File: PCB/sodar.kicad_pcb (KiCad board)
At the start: 2 copper layers, 70 parts, among them J1 Screw_Terminal_01x02, J2 Conn_02x12_Counter_Clockwise, J3 Conn_01x02, U1 TC78H621FNG, U10 TC78H621FNG, U2 TC78H621FNG, U3 TC78H621FNG, U4 TC78H621FNG, U5 TC78H621FNG, U6 TC78H621FNG, U7 TC78H621FNG, U8 TC78H621FNG, U9 TC78H621FNG

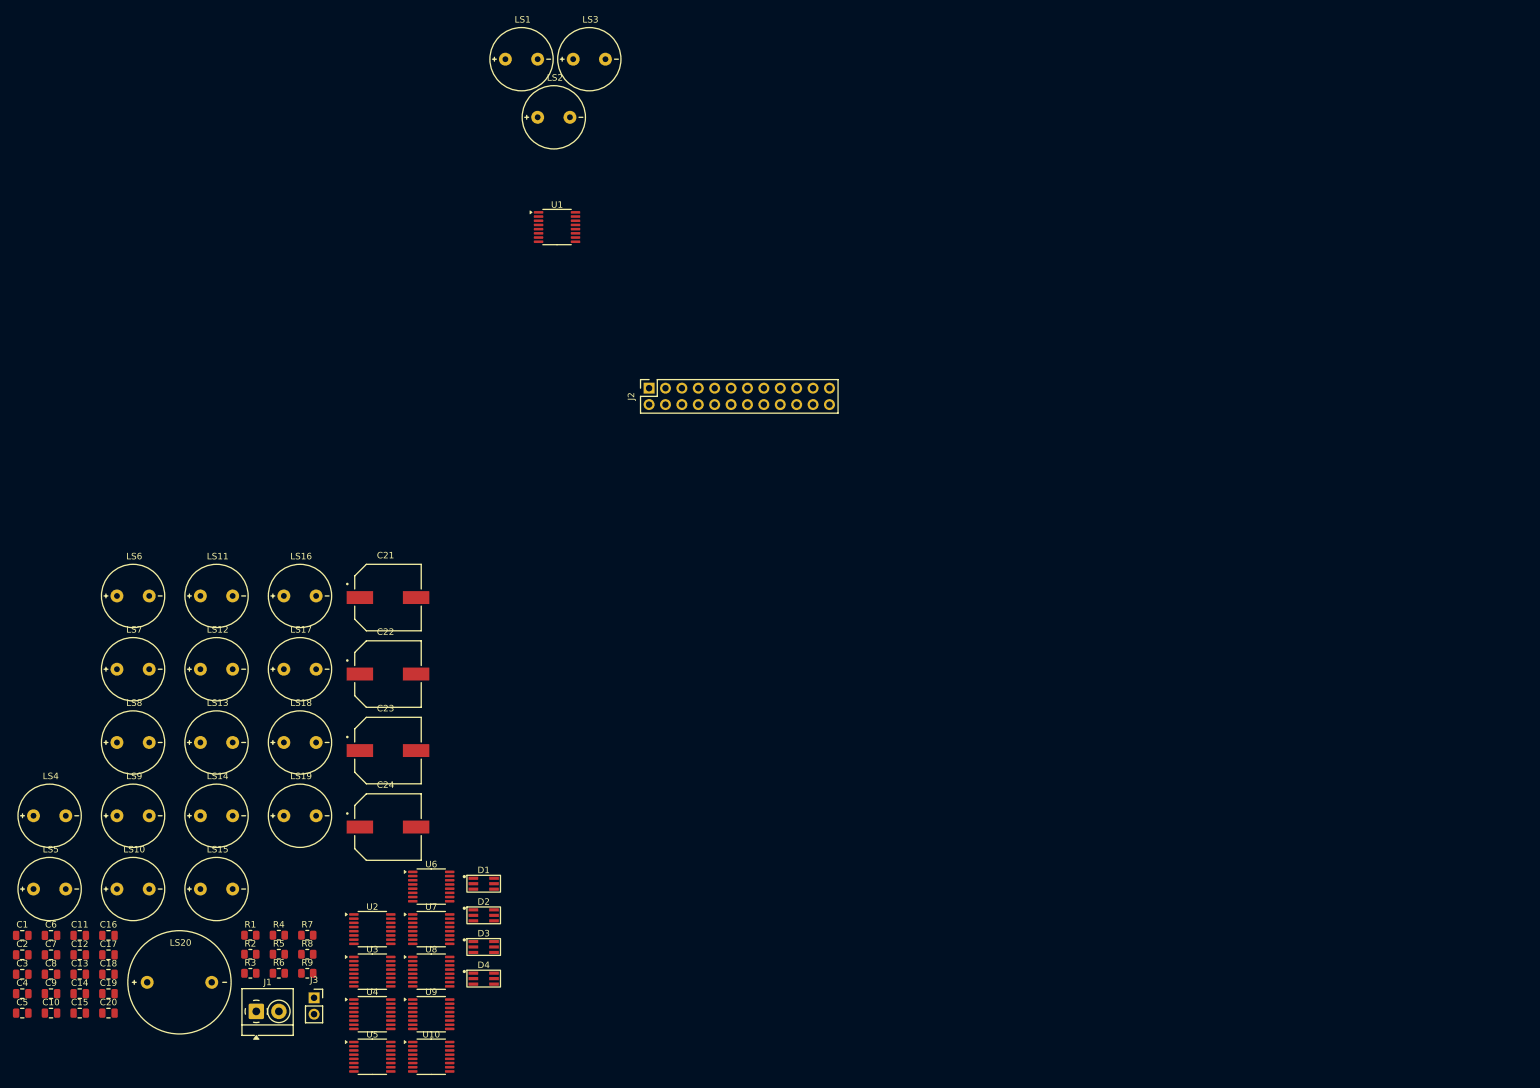
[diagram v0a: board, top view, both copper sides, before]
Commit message: Szymi pcb design (#5)
* updated transmiter footprint

* Moved the transducers and the drivers in the right positions

* first PCB layout finished, to be reviewed

---------

Co-authored-by: ads <ads>
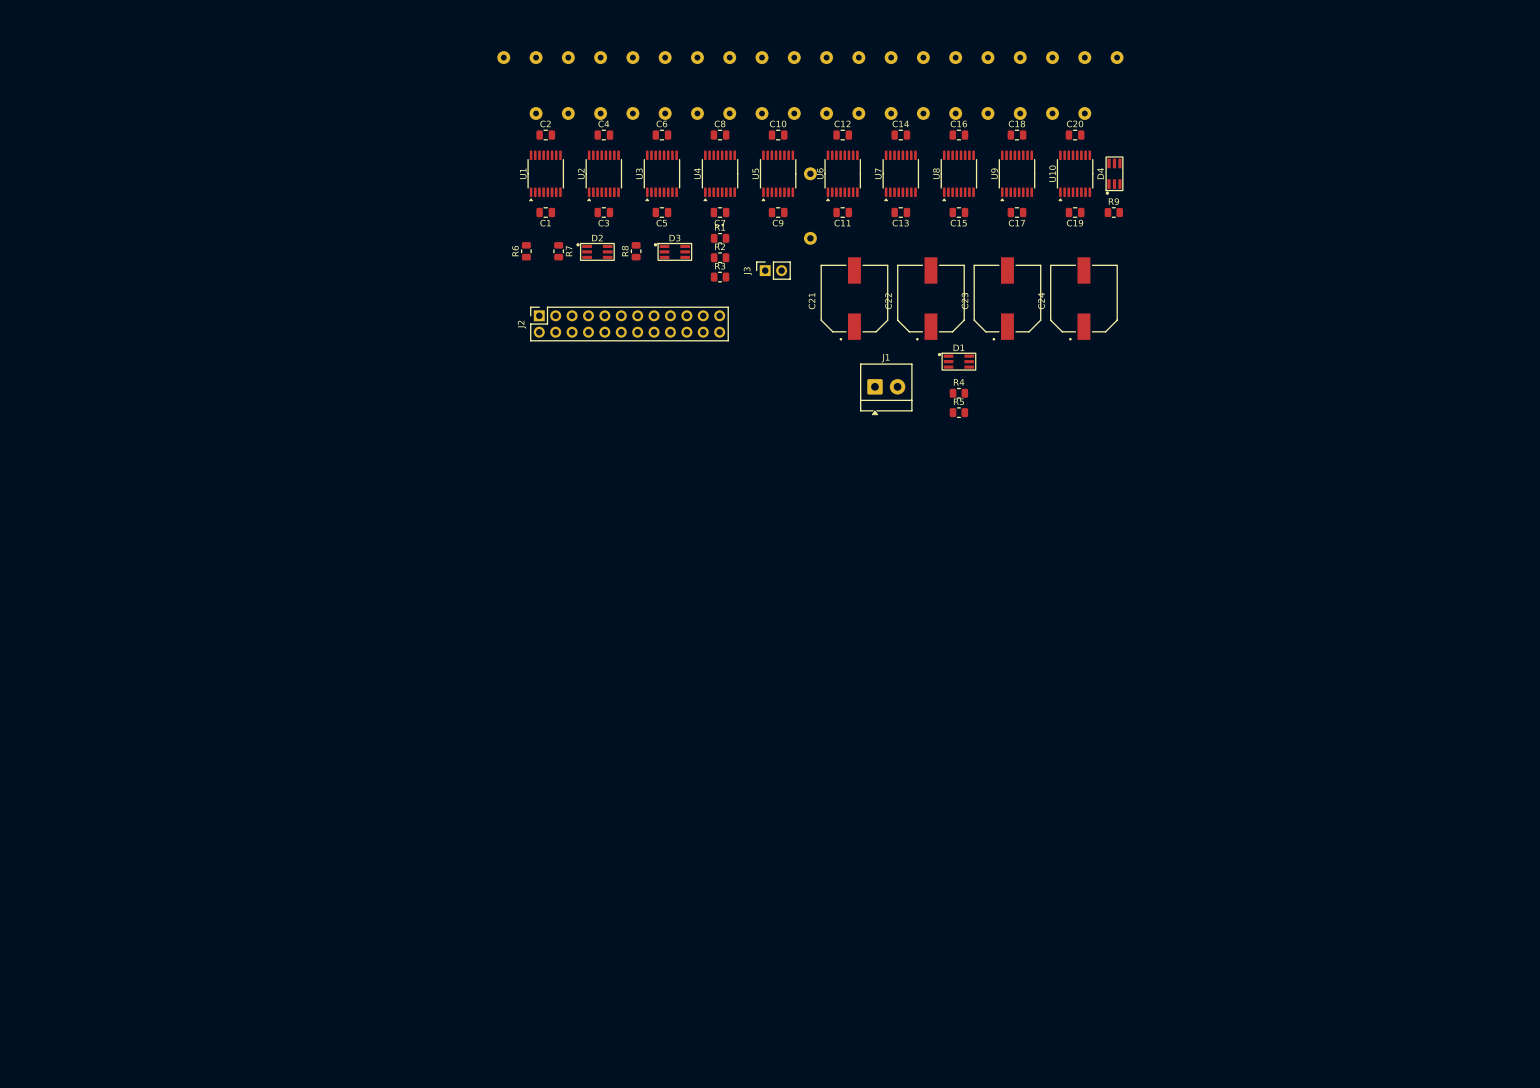
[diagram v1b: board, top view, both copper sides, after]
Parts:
- LS1, LS10, LS11, LS12, LS13, LS14, LS15, LS16, LS17, LS18, LS19, LS2, LS20, LS3, LS4, LS5, LS6, LS7, LS8, LS9: moved to B.Cu
- moved C20 202.3 mm to (191.0, 47.0)
- moved C19 192.5 mm to (191.0, 59.0), turned to 180 degrees
- moved C18 191.6 mm to (182.0, 47.0)
- moved C15 184.2 mm to (173.0, 59.0), turned to 180 degrees
- moved C14 184.0 mm to (164.0, 47.0)
- moved C17 181.7 mm to (182.0, 59.0), turned to 180 degrees
- moved C16 180.9 mm to (173.0, 47.0)
- moved C10 176.6 mm to (145.0, 47.0)
- moved LS15 174.0 mm to (175.0, 35.0)
- moved C13 173.5 mm to (164.0, 59.0), turned to 180 degrees
- moved C12 173.5 mm to (155.0, 47.0)
- moved R9 171.7 mm to (197.0, 59.0)
- moved LS19 170.8 mm to (195.0, 35.0)
- moved U10 169.3 mm to (191.0, 53.0), turned to 90 degrees
- moved C8 166.3 mm to (136.0, 47.0)
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
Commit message: Moved driver ICs
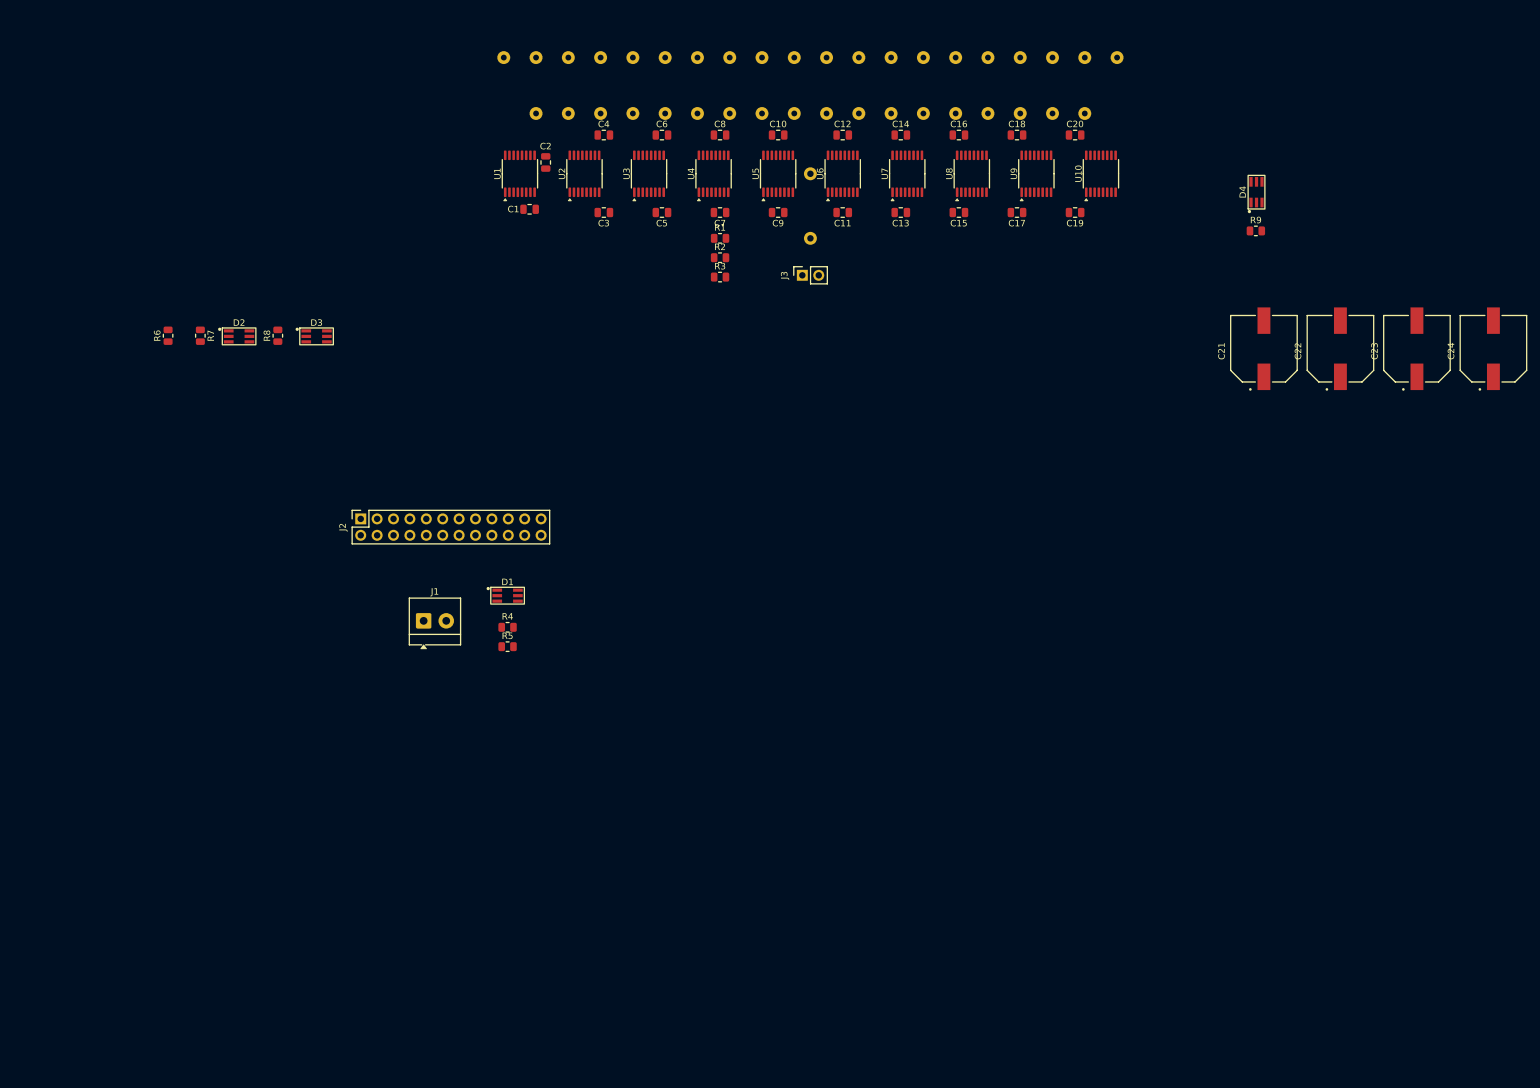
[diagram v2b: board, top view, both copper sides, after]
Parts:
- moved D1 78.8 mm to (103.1, 116.2)
- moved J1 78.8 mm to (90.1, 122.2)
- moved R4 78.8 mm to (103.1, 123.2)
- moved R5 78.8 mm to (103.1, 126.2)
- moved C21 63.9 mm to (220.2, 80.1)
- moved C22 63.9 mm to (232.1, 80.1)
- moved C24 63.9 mm to (255.8, 80.1)
- moved C23 63.9 mm to (243.9, 80.1)
- moved D2 57.0 mm to (61.5, 76.1)
- moved D3 57.0 mm to (73.5, 76.1)
- moved R6 57.0 mm to (50.5, 78.1)
- moved R7 57.0 mm to (55.5, 78.1)
- moved R8 57.0 mm to (67.5, 78.1)
- moved J2 41.9 mm to (80.3, 106.5)
- moved D4 22.2 mm to (217.0, 55.9)
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
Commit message: Better decoupling caps placement
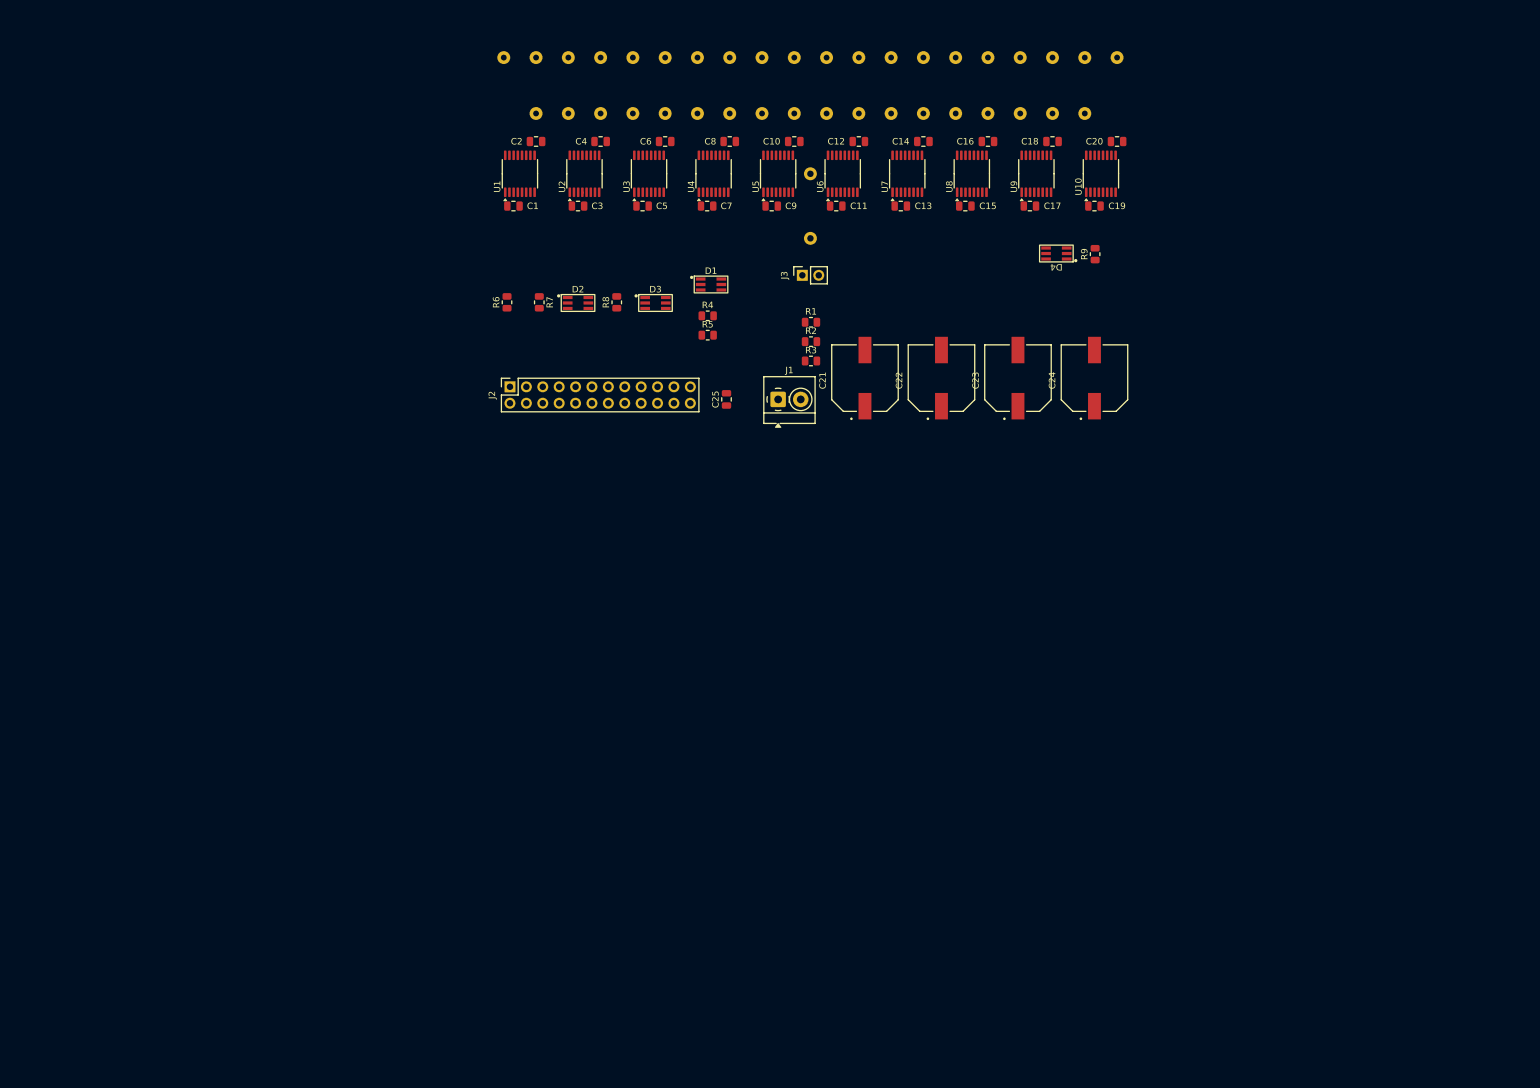
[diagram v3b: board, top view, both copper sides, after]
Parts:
- added C25: 10u, Capacitor_SMD:C_0805_2012Metric, F.Cu at (137.0, 88.0)
- moved J1 64.7 mm to (145.0, 88.0)
- moved C21 62.0 mm to (158.4, 84.7)
- moved C24 62.0 mm to (194.0, 84.7)
- moved C22 62.0 mm to (170.3, 84.7)
- moved C23 62.0 mm to (182.2, 84.7)
- moved D1 57.6 mm to (134.6, 68.0)
- moved R4 57.4 mm to (134.1, 75.0)
- moved R5 57.4 mm to (134.1, 78.0)
- moved D2 52.8 mm to (114.0, 70.9)
- moved D3 52.8 mm to (126.0, 70.9)
- moved R6 52.8 mm to (103.0, 72.9)
- moved R7 52.8 mm to (108.0, 72.9)
- moved R8 52.8 mm to (120.0, 72.9)
- moved D4 31.1 mm to (188.1, 67.5), turned to 180 degrees
- moved J2 30.9 mm to (103.5, 86.0)
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
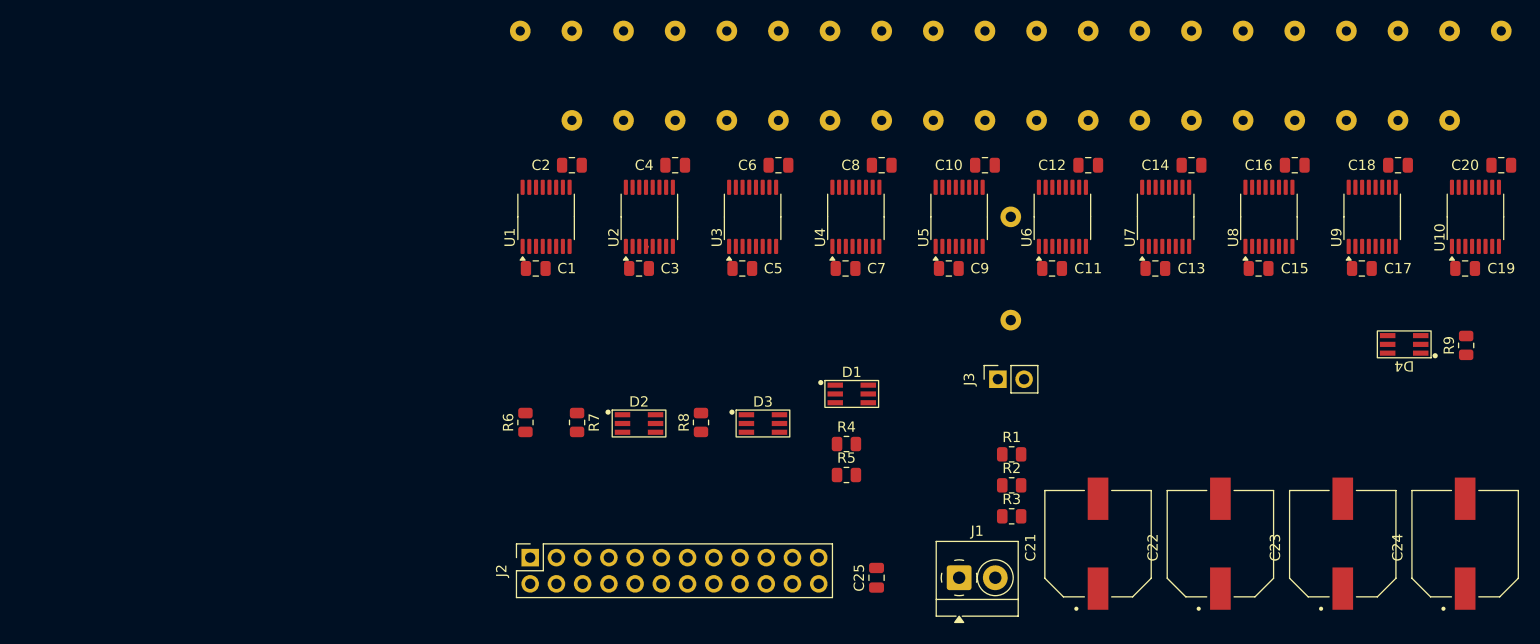
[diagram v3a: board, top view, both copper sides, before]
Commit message: Routed transducers and decoup caps to the ICs
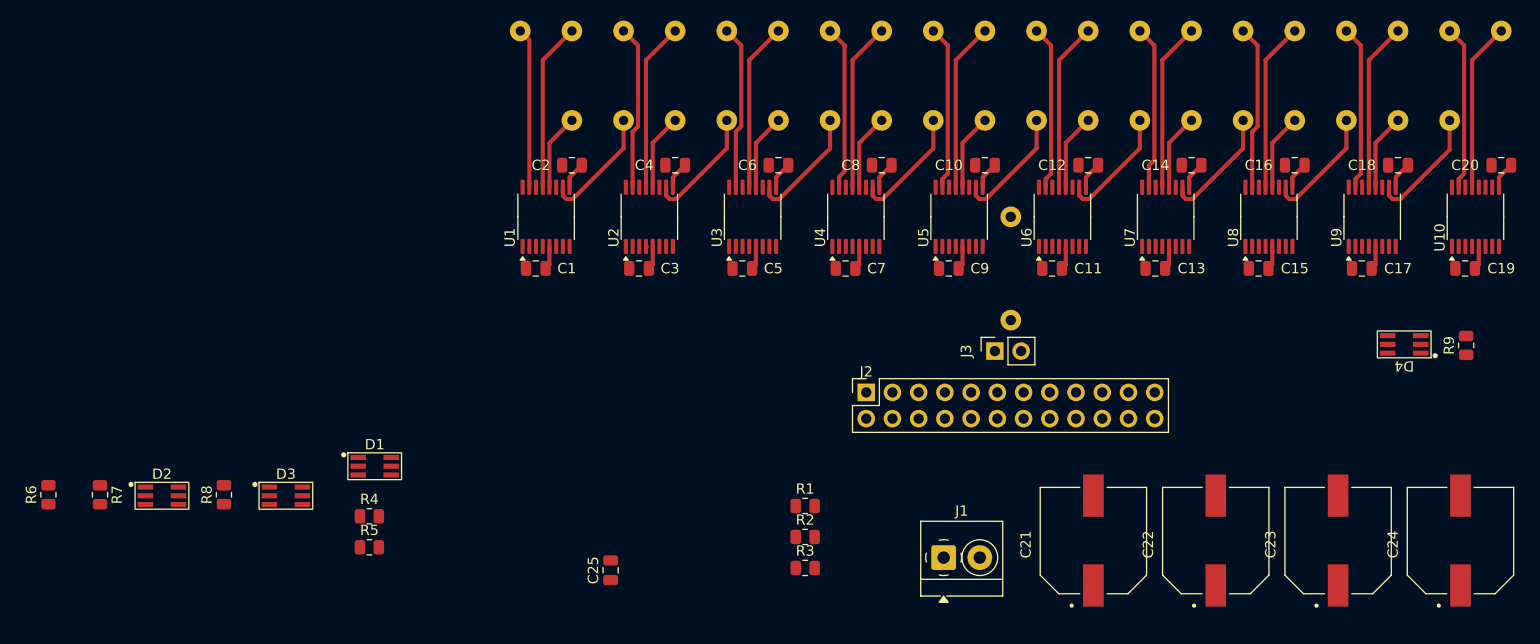
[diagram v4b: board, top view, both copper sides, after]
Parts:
- moved D2 46.7 mm to (67.8, 77.9)
- moved D3 46.7 mm to (79.8, 77.9)
- moved R4 46.7 mm to (87.9, 82.0)
- moved R5 46.7 mm to (87.9, 85.0)
- moved R6 46.7 mm to (56.8, 79.9)
- moved R7 46.7 mm to (61.8, 79.9)
- moved R8 46.7 mm to (73.8, 79.9)
- moved D1 46.7 mm to (88.4, 75.0)
- moved J2 36.3 mm to (136.0, 70.0)
- moved C25 25.8 mm to (111.2, 87.2)
- moved R1 20.6 mm to (130.1, 81.0)
- moved R2 20.6 mm to (130.1, 84.0)
- moved R3 20.6 mm to (130.1, 87.0)
- moved J3 2.74 mm to (148.5, 66.0)
- moved J1 2.46 mm to (143.5, 86.0)
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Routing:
- net Vdrive: track 0.00 -> 26.2 mm
- net +3V3: track 0.00 -> 22.9 mm
- net Net-(U3-AO2): track 0.00 -> 16.3 mm
- net Net-(U2-AO2): track 0.00 -> 16.3 mm
- net Net-(U1-AO2): track 0.00 -> 16.3 mm
- net Net-(U9-AO2): track 0.00 -> 16.3 mm
- net Net-(U8-AO2): track 0.00 -> 16.3 mm
- net Net-(U7-AO2): track 0.00 -> 16.3 mm
- net Net-(U6-AO2): track 0.00 -> 16.3 mm
- net Net-(U5-AO2): track 0.00 -> 16.3 mm
- net Net-(U4-AO2): track 0.00 -> 16.3 mm
- net Net-(U10-AO2): track 0.00 -> 16.3 mm
- net Net-(U10-AO1): track 0.00 -> 15.9 mm
- net Net-(U9-AO1): track 0.00 -> 15.9 mm
- net Net-(U7-AO1): track 0.00 -> 15.9 mm
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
